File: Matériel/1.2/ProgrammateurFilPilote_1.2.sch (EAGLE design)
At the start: 78 parts, among them IC2 MCP23017, J2 GROVE-I2C, P1 PADSMALL, P2 PADSMALL, SW1 HLS8L-DC5V-S-C, T1 2N2222

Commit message: Revert "Màj v1.2"
This reverts commit 1069f649c9f2bcb6078a36c473411e82ae330c49.
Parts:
- removed J2: GROVE-I2C, seeed-opl-Connector:GROVE-4P-2.0-3470130P1
- removed RL: (no value), con-ptr500:AK500/2
- removed SW1: HLS8L-DC5V-S-C, seeed-opl-Connector:RELAY-HLS8L-DC5V-S-C-315030000
- added CONTACT_SEC: (no value), con-ptr500:AK500/2
- D1, D10, D11, D12, D13, D14, D2, D3, D4, D5, D6, D7, D8, D9: value SL1J -> CGRM4001-G; device seeed-opl-Discrete:DIODE-SMA -> diode:CGRM4001-G
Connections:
- removed net COM: RELAIS2.P, RL-1.KL, SW1.COM
- removed net N$16: 230V-1.KL, F1.1
- removed net NF: RL-2.KL, SW1.NC
- removed net NO: 230V-2.KL, RELAIS2.S, SW1.NO
- new net N$17: 230V-2.KL, F1.1
- new net N$18: CONTACT_SEC-2.KL, RELAIS2.S
- new net N$20: CONTACT_SEC-1.KL, RELAIS2.P
- new net NEUTRE: 230V-1.KL
- net +3V3: no longer J2.2
- net +5V: no longer SW1.V+
- net FP1: now also D1.A, D2.C; no longer D1.+, D2.-
- net FP2: now also D3.A, D4.C; no longer D3.+, D4.-
- net FP3: now also D5.A, D6.C; no longer D5.+, D6.-
- net FP4: now also D7.A, D8.C; no longer D7.+, D8.-
- net FP5: now also D10.C, D9.A; no longer D10.-, D9.+
- net FP6: now also D11.A, D12.C; no longer D11.+, D12.-
- net FP7: now also D13.A, D14.C; no longer D13.+, D14.+
- net GND: no longer J2.1
- net N$1: now also D1.C; no longer D1.-
- net N$15: no longer SW1.V-
- net N$2: now also D2.A; no longer D2.+
- net N$22: now also D3.C; no longer D3.-
- net N$24: now also D5.C; no longer D5.-
- net N$25: now also D4.A; no longer D4.+
- net N$26: now also D7.C; no longer D7.-
- net N$29: now also D6.A; no longer D6.+
- net N$31: now also D8.A; no longer D8.+
- net N$42: now also D9.C; no longer D9.-
- net N$49: now also D10.A; no longer D10.+
- net N$51: now also D12.A; no longer D12.+
- net S$1: now also D11.C; no longer D11.-
- net S$11: now also D14.A; no longer D14.-
- net S$3: now also D13.C; no longer D13.-
- net SCL: no longer J2.4
- net SDA: no longer J2.3
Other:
- note removed: "7 Fils pilotes + 2 type de relais (au choix)"
- note removed: "A"
- note removed: "Double Récepteur RFM69 ou RFM12B + 433MHz"
- note removed: "Module au choix, RFM12B, RFM69CW"
- note removed: "Ou RFM69HW"
- note removed: "Récepteur 433MHz"
- moved on the sheet: 230V-1, C1, D15, EXTENSION-1, EXTENSION-2, EXTENSION-3, EXTENSION-4, EXTENSION-5, F1, I2C_OLED, IC2, JP3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

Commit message: Màj v1.2
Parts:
- removed CONTACT_SEC: (no value), con-ptr500:AK500/2
- added J2: GROVE-I2C, seeed-opl-Connector:GROVE-4P-2.0-3470130P1
- added RL: (no value), con-ptr500:AK500/2
- added SW1: HLS8L-DC5V-S-C, seeed-opl-Connector:RELAY-HLS8L-DC5V-S-C-315030000
- D1, D10, D11, D12, D13, D14, D2, D3, D4, D5, D6, D7, D8, D9: value CGRM4001-G -> SL1J; device diode:CGRM4001-G -> seeed-opl-Discrete:DIODE-SMA
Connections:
- removed net N$17: 230V-2.KL, F1.1
- removed net N$18: CONTACT_SEC-2.KL, RELAIS2.S
- removed net N$20: CONTACT_SEC-1.KL, RELAIS2.P
- removed net NEUTRE: 230V-1.KL
- new net COM: RELAIS2.P, RL-1.KL, SW1.COM
- new net N$16: 230V-1.KL, F1.1
- new net NF: RL-2.KL, SW1.NC
- new net NO: 230V-2.KL, RELAIS2.S, SW1.NO
- net +3V3: now also J2.2
- net +5V: now also SW1.V+
- net FP1: now also D1.+, D2.-; no longer D1.A, D2.C
- net FP2: now also D3.+, D4.-; no longer D3.A, D4.C
- net FP3: now also D5.+, D6.-; no longer D5.A, D6.C
- net FP4: now also D7.+, D8.-; no longer D7.A, D8.C
- net FP5: now also D10.-, D9.+; no longer D10.C, D9.A
- net FP6: now also D11.+, D12.-; no longer D11.A, D12.C
- net FP7: now also D13.+, D14.+; no longer D13.A, D14.C
- net GND: now also J2.1
- net N$1: now also D1.-; no longer D1.C
- net N$15: now also SW1.V-
- net N$2: now also D2.+; no longer D2.A
- net N$22: now also D3.-; no longer D3.C
- net N$24: now also D5.-; no longer D5.C
- net N$25: now also D4.+; no longer D4.A
- net N$26: now also D7.-; no longer D7.C
- net N$29: now also D6.+; no longer D6.A
- net N$31: now also D8.+; no longer D8.A
- net N$42: now also D9.-; no longer D9.C
- net N$49: now also D10.+; no longer D10.A
- net N$51: now also D12.+; no longer D12.A
- net S$1: now also D11.-; no longer D11.C
- net S$11: now also D14.-; no longer D14.A
- net S$3: now also D13.-; no longer D13.C
- net SCL: now also J2.4
- net SDA: now also J2.3
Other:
- note added: "7 Fils pilotes + 2 type de relais (au choix)"
- note added: "A"
- note added: "Double Récepteur RFM69 ou RFM12B + 433MHz"
- note added: "Module au choix, RFM12B, RFM69CW"
- note added: "Ou RFM69HW"
- note added: "Récepteur 433MHz"
- moved on the sheet: 230V-1, C1, D15, EXTENSION-1, EXTENSION-2, EXTENSION-3, EXTENSION-4, EXTENSION-5, F1, I2C_OLED, IC2, JP3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

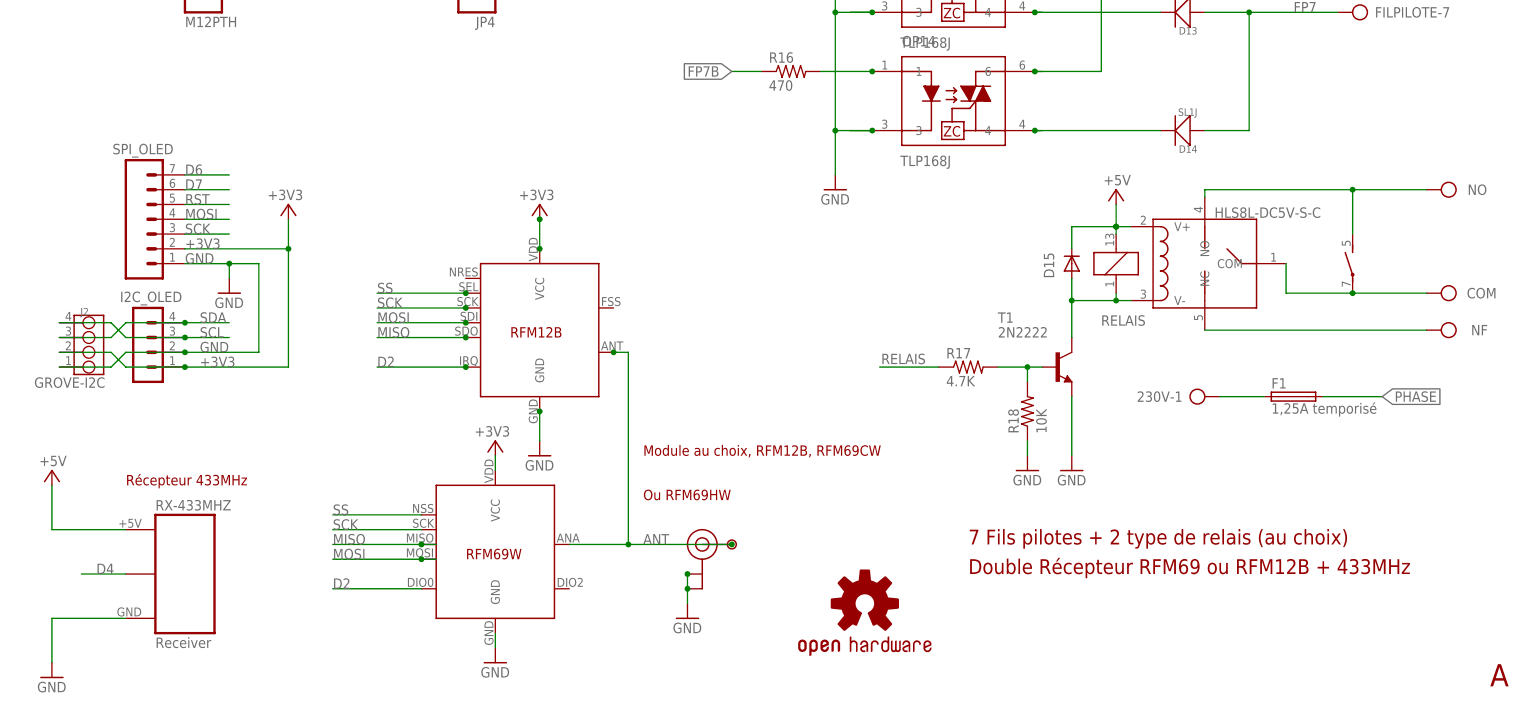
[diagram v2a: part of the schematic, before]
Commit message: Passage en Révision 1.2b
Correction d'inversion du sens du connecteur Grove
Correction d'inversion diode D14
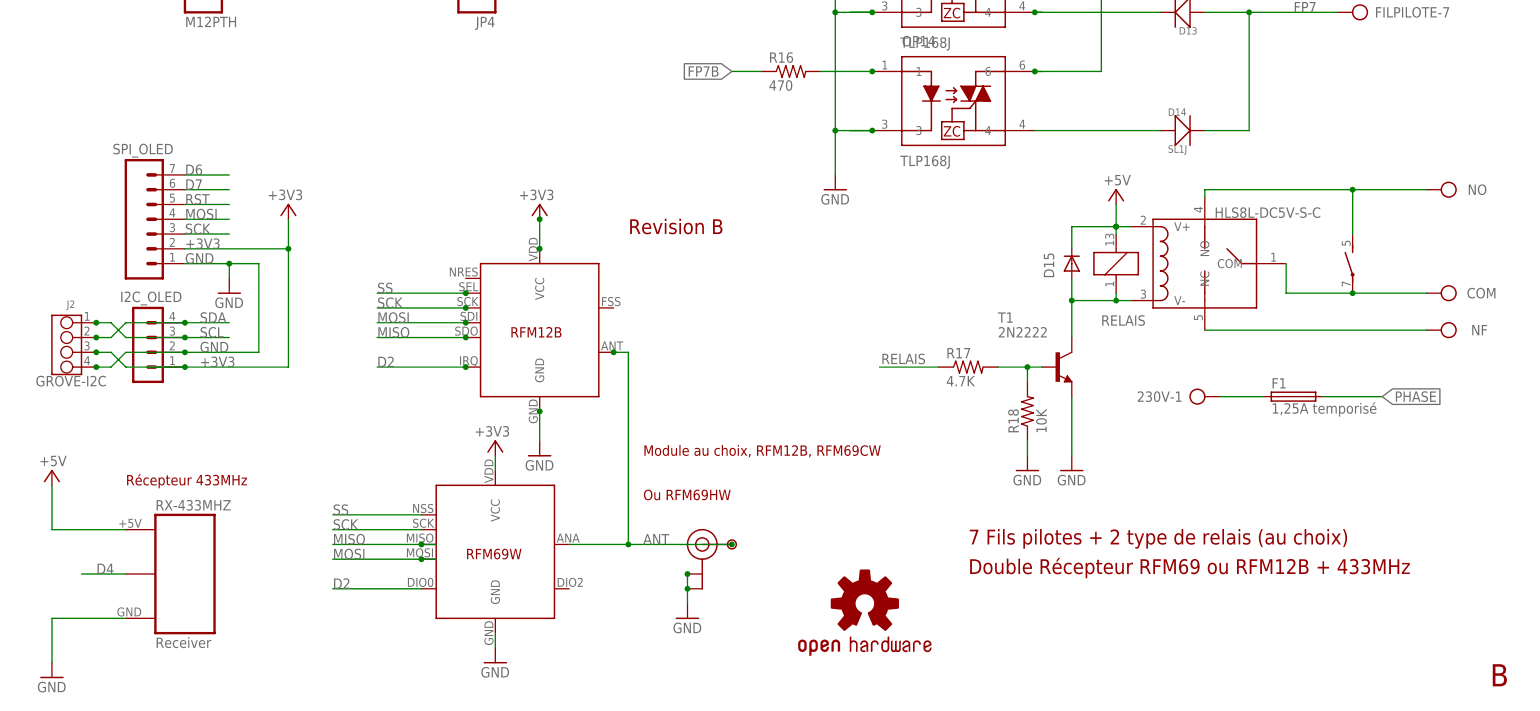
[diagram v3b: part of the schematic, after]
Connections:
- net +3V3: now also J2.3; no longer J2.2
- net FP7: now also D14.-; no longer D14.+
- net GND: now also J2.4; no longer J2.1
- net S$11: now also D14.+; no longer D14.-
- net SCL: now also J2.1; no longer J2.4
- net SDA: now also J2.2; no longer J2.3
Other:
- note added: "B"
- note added: "Revision B"
- note removed: "A"
- moved on the sheet: D14, J2
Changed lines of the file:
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@@
 <plain>
 <text x="-35.56" y="-106.68" size="2.54" layer="94">7 Fils pilotes + 2 type de relais (au choix)</text>
-<text x="54.102" y="-131.064" size="3.81" layer="94">A</text>
+<text x="54.102" y="-131.064" size="3.81" layer="94">B</text>
 <text x="-91.44" y="-91.44" size="1.778" layer="94">Module au choix, RFM12B, RFM69CW</text>
 <text x="-91.44" y="-99.06" size="1.778" layer="94">Ou RFM69HW</text>
 <text x="-180.34" y="-96.52" size="1.778" layer="94">Récepteur 433MHz</text>
 <text x="-35.56" y="-111.76" size="2.54" layer="94">Double Récepteur RFM69 ou RFM12B + 433MHz</text>
+<text x="-93.98" y="-53.34" size="2.54" layer="94">Revision B</text>
 </plain>
 <instances>
@@
 <instance part="D12" gate="D" x="1.27" y="5.08"/>
 <instance part="D13" gate="D" x="1.27" y="-15.24" rot="R180"/>
-<instance part="D14" gate="D" x="1.27" y="-35.56" rot="R180"/>
-<instance part="J2" gate="J" x="-186.69" y="-72.39" smashed="yes" rot="R180">
-<attribute name="NAME" x="-186.69" y="-66.04" size="1.27" layer="95" ratio="10" rot="R180"/>
-<attribute name="VALUE" x="-196.088" y="-77.978" size="1.778" layer="96" ratio="10" rot="MR180"/>
+<instance part="D14" gate="D" x="1.27" y="-35.56"/>
+<instance part="J2" gate="J" x="-190.5" y="-72.39" smashed="yes">
+<attribute name="NAME" x="-190.5" y="-66.04" size="1.27" layer="95" ratio="10"/>
+<attribute name="VALUE" x="-183.642" y="-79.502" size="1.778" layer="96" ratio="10" rot="MR0"/>
 </instance>
 <instance part="FRAME1" gate="G$1" x="-200.66" y="-137.16"/>
@@
 <label x="-167.64" y="-73.66" size="1.778" layer="95"/>
 <wire x1="-180.34" y1="-73.66" x2="-182.88" y2="-76.2" width="0.1524" layer="91"/>
-<pinref part="J2" gate="J" pin="1"/>
-<wire x1="-182.88" y1="-76.2" x2="-191.77" y2="-76.2" width="0.1524" layer="91"/>
 <wire x1="-170.18" y1="-73.66" x2="-180.34" y2="-73.66" width="0.1524" layer="91"/>
 <junction x="-170.18" y="-73.66"/>
+<pinref part="J2" gate="J" pin="4"/>
+<wire x1="-182.88" y1="-76.2" x2="-185.42" y2="-76.2" width="0.1524" layer="91"/>
+<junction x="-185.42" y="-76.2"/>
 </segment>
 <segment>
@@
 <pinref part="I2C_OLED" gate="G$1" pin="3"/>
 <wire x1="-170.18" y1="-71.12" x2="-162.56" y2="-71.12" width="0.1524" layer="91"/>
-<pinref part="J2" gate="J" pin="4"/>
-<wire x1="-191.77" y1="-68.58" x2="-182.88" y2="-68.58" width="0.1524" layer="91"/>
 <wire x1="-182.88" y1="-68.58" x2="-180.34" y2="-71.12" width="0.1524" layer="91"/>
 <wire x1="-180.34" y1="-71.12" x2="-170.18" y2="-71.12" width="0.1524" layer="91"/>
 <junction x="-170.18" y="-71.12"/>
+<pinref part="J2" gate="J" pin="1"/>
+<wire x1="-182.88" y1="-68.58" x2="-185.42" y2="-68.58" width="0.1524" layer="91"/>
+<junction x="-185.42" y="-68.58"/>
 </segment>
 <segment>
@@
 <label x="-170.18" y="-55.88" size="1.778" layer="95"/>
 <label x="-167.64" y="-76.2" size="1.778" layer="95"/>
-<pinref part="J2" gate="J" pin="2"/>
-<wire x1="-191.77" y1="-73.66" x2="-182.88" y2="-73.66" width="0.1524" layer="91"/>
 <wire x1="-182.88" y1="-73.66" x2="-180.34" y2="-76.2" width="0.1524" layer="91"/>
 <wire x1="-180.34" y1="-76.2" x2="-170.18" y2="-76.2" width="0.1524" layer="91"/>
 <junction x="-170.18" y="-76.2"/>
+<pinref part="J2" gate="J" pin="3"/>
+<wire x1="-182.88" y1="-73.66" x2="-185.42" y2="-73.66" width="0.1524" layer="91"/>
+<junction x="-185.42" y="-73.66"/>
 </segment>
 <segment>
@@
 <wire x1="-170.18" y1="-68.58" x2="-180.34" y2="-68.58" width="0.1524" layer="91"/>
 <wire x1="-180.34" y1="-68.58" x2="-182.88" y2="-71.12" width="0.1524" layer="91"/>
-<pinref part="J2" gate="J" pin="3"/>
-<wire x1="-182.88" y1="-71.12" x2="-191.77" y2="-71.12" width="0.1524" layer="91"/>
 <junction x="-170.18" y="-68.58"/>
+<pinref part="J2" gate="J" pin="2"/>
+<wire x1="-182.88" y1="-71.12" x2="-185.42" y2="-71.12" width="0.1524" layer="91"/>
+<junction x="-185.42" y="-71.12"/>
 </segment>
 <segment>
@@
 <segment>
 <wire x1="5.08" y1="-15.24" x2="12.7" y2="-15.24" width="0.1524" layer="91"/>
-<wire x1="5.08" y1="-35.56" x2="12.7" y2="-35.56" width="0.1524" layer="91"/>
 <wire x1="12.7" y1="-35.56" x2="12.7" y2="-15.24" width="0.1524" layer="91"/>
 <wire x1="27.94" y1="-15.24" x2="12.7" y2="-15.24" width="0.1524" layer="91"/>
@@
 <label x="20.32" y="-15.24" size="1.778" layer="95"/>
 <pinref part="D13" gate="D" pin="+"/>
+<pinref part="D14" gate="D" pin="-"/>
+<wire x1="5.08" y1="-35.56" x2="12.7" y2="-35.56" width="0.1524" layer="91"/>
+</segment>
+</net>
+<net name="S$11" class="0">
+<segment>
+<pinref part="OP14" gate="G$1" pin="4"/>
 <pinref part="D14" gate="D" pin="+"/>
-</segment>
-</net>
-<net name="S$11" class="0">
-<segment>
-<wire x1="-22.86" y1="-35.56" x2="-24.13" y2="-35.56" width="0.1524" layer="91"/>
-<pinref part="OP14" gate="G$1" pin="4"/>
-<wire x1="-24.13" y1="-35.56" x2="-2.54" y2="-35.56" width="0.1524" layer="91"/>
-<junction x="-24.13" y="-35.56"/>
-<pinref part="D14" gate="D" pin="-"/>
-</segment>
-</net>
+<wire x1="-2.54" y1="-35.56" x2="-24.13" y2="-35.56" width="0.1524" layer="91"/>
+</segment>
+</net>

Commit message: Révision 1.2c
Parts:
- OP1, OP10, OP11, OP12, OP13, OP14, OP2, OP3, OP4, OP5, OP6, OP7, OP8, OP9: device TLP168J:TLP168J -> TLP168J:TLP168JBIGPAD
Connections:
- net +3V3: now also EXTENSION-5.KL; no longer EXTENSION-4.KL
- net GND: now also EXTENSION-4.KL; no longer EXTENSION-5.KL
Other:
- note added: "C"
- note removed: "B"
